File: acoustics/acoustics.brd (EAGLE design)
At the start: 160 x 100 mm, 172 parts, among them X1 22-23-2021, X2 22-23-2021, X3 22-23-2021

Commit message: Combining AGND and GND into one
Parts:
- removed C1, C10, C11, C12, C13, C14, C2, C3, C4, C47, C5, C6, C7, C9: 1uf, rcl:C0805K
- removed C48, C8: 10uf, rcl:C0805K
- removed C74, C76: 0.1uf, rcl:C0805K
- removed C75, C77: 47uf, rcl:C0805K
- removed R1, R2: 60.4k, rcl:M0805
- removed R3, R4: 10K, rcl:M0805
- removed R67, R68: 121k, resistor:R0603
- removed R71, R72: 47m, resistor:R0603
- added H2ADC_C9, H3ADC_C9: 0.1uf, rcl:C0603
- added H2RF_C1, H3RF_C1: 10uf, rcl:C0603
- added H2RF_C4, H2_C1, H2_C11, H2_C2, H2_C25, H2_C27, H2_C6, H3RF_C4, H3_ADC_C5, H3_C1, H3_C11, H3_C2, H3_C25, H3_C27: 1uf, rcl:C0603
- added H2RF_C6, H3RF_C6: 47uf, rcl:C0603
- added H2RF_R3, H3RF_R3: 121k, resistor:R0603
- added H2RF_RO, H3RF_RO: 47m, resistor:R0603
- added H2_R7, H3_R7: 60.4k, rcl:R0603
- added H2_R8, H3_R8: 10K, rcl:R0603
- moved U$10 292.7 mm to (71.6, 54.0)
- moved U$11 285.8 mm to (71.6, 30.6)
- moved H3CON 136.8 mm to (86.5, 41.1), turned to 270 degrees
- moved H2CON 133.1 mm to (86.5, 64.5), turned to 270 degrees
- moved ADC_H1 127.2 mm to (74.6, 92.6)
- moved ADC_H2 119.1 mm to (74.8, 65.4)
- moved ADC_H3 118.8 mm to (74.8, 42.1)
- moved U$2 35.2 mm to (-70.6, 47.6)
- moved H4_IN 29.9 mm to (39.5, 11.6), turned to 180 degrees
- moved H4_OUT 22.4 mm to (86.5, 18.3)
- moved H4PA_C_IN 22.2 mm to (38.3, 17.1), turned to 90 degrees
- moved ADC_H4 21.1 mm to (74.8, 19.1)
- moved H4DA_R_ON1 21.1 mm to (54.8, 20.6)
- moved H4DA_R_OP1 21.1 mm to (54.8, 18.7)
- moved H4RF_C_4 21.1 mm to (73.8, 6.03)
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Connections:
- new net N$37: ADC_H3.9, H3ADC_C9.2, H3RF_C6.2, U$11.5, U$11.6
- new net N$6: ADC_H1.9, C25.2, C73.2, U$1.5, U$1.6
- net +3V3: now also H2RF_C1.2, H2_C27.1, H2_C6.2, H3RF_C1.2, H3_ADC_C5.1, H3_C27.1; no longer C10.1, C11.2, C12.1, C13.1, C48.2, C8.2
- net AGND: no longer ADC_H1.10, ADC_H1.31, ADC_H1.5, ADC_H2.10, ADC_H2.31, ADC_H2.5, ADC_H3.10, ADC_H3.31, ADC_H3.5, ADC_H4.10, ADC_H4.31, ADC_H4.5, C1.1, C10.2, C11.1, C2.1, C22.1, C23.1, C24.2, C25.1, C26.2, C29.1, C3.1, C30.1, C31.1, C39.1, C4.2, C41.2, C47.1, C48.1, C54.1, C55.2, C6.1, C7.1, C74.1, C76.1, C8.1, C9.2, H4ADC_C.2, H4DA_R_IN1.1, H4RF_C_4.1, H4RF_C_IN.1, H4RF_C_O2.1, H4RF_R_0.1, H4RF_R_3.1, H4_C1.1, H4_C11.2, H4_C2.1, H4_DIFAMP.6, H4_IN.1, H4_PREAMP.2, H4_R6.2, H4_R7.2, H4_REFGEN.7, H4_REFGEN.8, HFPA_C.1, HFPA_C_INP.2, HFPA_R.2, R1.2, R15.1, R2.2, R24.2, R29.1, R3.2, R36.2, R4.2, R41.1, R65.1, R66.1, R67.1, R68.1, R7.2, R71.1, R72.1, R8.2, U$1.7, U$1.8, U$10.7, U$10.8, U$11.7, U$11.8, U$2.6, U$3.6, U$4.2, U$5.6, U$6.2, U$7.2, X1.1, X2.1, X3.1
- net GND: now also ADC_H1.10, ADC_H1.31, ADC_H1.5, ADC_H2.10, ADC_H2.12, ADC_H2.13, ADC_H2.14, ADC_H2.15, ADC_H2.16, ADC_H2.18, ADC_H2.21, ADC_H2.31, ADC_H2.5, ADC_H3.10, ADC_H3.12, ADC_H3.13, ADC_H3.14, ADC_H3.15, ADC_H3.16, ADC_H3.18, ADC_H3.21, ADC_H3.31, ADC_H3.5, ADC_H4.10, ADC_H4.31, ADC_H4.5, C22.1, C23.1, C24.2, C25.1, C26.2, C29.1, C30.1, C31.1, C39.1, C41.2, C54.1, C55.2, H2ADC_C9.1, H2RF_C1.1, H2RF_C4.1, H2RF_R3.1, H2RF_RO.1, H2_C1.1, H2_C11.2, H2_C2.1, H2_C25.1, H2_C27.2, H2_C6.1, H2_R7.2, H2_R8.2, H3ADC_C9.1, H3RF_C1.1, H3RF_C4.1, H3RF_R3.1, H3RF_RO.1, H3_ADC_C5.2, H3_C1.1, H3_C11.2, H3_C2.1, H3_C25.1, H3_C27.2, H3_R7.2, H3_R8.2, H4ADC_C.2, H4DA_R_IN1.1, H4RF_C_4.1, H4RF_C_IN.1, H4RF_C_O2.1, H4RF_R_0.1, H4RF_R_3.1, H4_C1.1, H4_C11.2, H4_C2.1, H4_DIFAMP.6, H4_IN.1, H4_PREAMP.2, H4_R6.2, H4_R7.2, H4_REFGEN.7, H4_REFGEN.8, HFPA_C.1, HFPA_C_INP.2, HFPA_R.2, R15.1, R24.2, R29.1, R36.2, R41.1, R65.1, R66.1, R7.2, R8.2, U$1.7, U$1.8, U$10.7, U$10.8, U$11.7, U$11.8, U$2.6, U$3.6, U$4.2, U$5.6, U$6.2, U$7.2, X1.1, X2.1, X3.1; no longer ADC_H4.24, C12.2, C13.2, C14.1, C5.1
- net N$1: now also H2_C1.2; no longer C2.2
- net N$12: now also H3_C1.2; no longer C7.2
- net N$13: now also H2_C25.2; no longer C5.2
- net N$18: now also H3_R7.1; no longer R2.1
- net N$21: now also H3_C11.1; no longer C9.1
- net N$22: now also H2_R8.1; no longer R3.1
- net N$23: now also H3_R8.1; no longer R4.1
- net N$3: now also H2_C2.2; no longer C1.2
- net N$30: now also H3_C25.2; no longer C14.2
- net N$4: now also H2_R7.1; no longer R1.1
- net N$42: now also H2RF_C4.2; no longer C3.2
- net N$43: now also H2RF_R3.2; no longer R67.2
- net N$47: now also H3RF_C4.2; no longer C47.2
- net N$79: now also H3RF_R3.2; no longer R68.2
- net N$8: now also H3_C2.2; no longer C6.2
- net N$86: now also H2RF_C6.1, H2RF_RO.2; no longer C75.1, R71.2
- net N$87: now also H3RF_C6.1, H3RF_RO.2; no longer C77.1, R72.2
- net N$9: now also H2_C11.1; no longer C4.1
- net POSITIVE_REF: now also H2ADC_C9.2, H2RF_C6.2; no longer ADC_H1.9, ADC_H3.9, C25.2, C73.2, C74.2, C75.2, C76.2, C77.2, U$1.5, U$1.6, U$11.5, U$11.6
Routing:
- net START: track 3.96 -> 85.5 mm, vias 1 -> 3
- net GND: track 12.7 -> 91.0 mm, vias 9 -> 74
- net SCLK: track 5.90 -> 79.9 mm, vias 1 -> 3
- net AGND: track 22.5 -> 0.00 mm, vias 21 -> 0
- net +3V3: track 15.0 -> 36.0 mm, vias 9 -> 21
- net DRDY_H3: track 0.00 -> 7.88 mm
- net DRDY_H2: track 0.00 -> 7.88 mm
- net DOUT_H2: track 0.00 -> 7.82 mm
- net DOUT_H3: track 0.00 -> 7.75 mm
- net N$54: track 10.0 -> 2.82 mm
- net N$37: track 0.00 -> 7.20 mm
- net POSITIVE_REF: track 0.00 -> 5.52 mm
- net N$71: track 8.57 -> 3.85 mm
- net DOUT_H4: track 10.1 -> 7.82 mm
- net DRDY_H4: track 9.97 -> 7.91 mm
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- removed copper zone on layer 2, net AGND
- removed copper zone on layer 2, net GND
- removed copper zone on layer 15, net N$37
- removed copper zone on layer 16, net N$41
- removed copper zone on layer 1, net N$88
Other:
- board size 160 x 100 mm -> 127 x 101.6 mm

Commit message: Initial placement of parts completed
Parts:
- removed C22, C23, C24, C26, C27, C28, C29: 1uf, rcl:C0805K
- removed C25: 0.1uf, rcl:C0805K
- removed C30: 10uf, rcl:C0805K
- removed C31, C39, C54: 100nF, resistor:C0603
- removed C32, C36, C44, C45, C58, C59: 270pF, resistor:C0603
- removed C33, C41, C55: 10mF, resistor:C0603
- removed C34, C42, C56: 1pF, resistor:C0603
- removed C35, C43, C57: 5nF, resistor:C0603
- removed C37, C46, C60: 1nF, resistor:C0603
- removed C38, C53, C61: 470 pF, resistor:C0603
- removed C40, C62, C71: 22nF, resistor:C0603
- removed C73: 47uf, rcl:C0805K
- removed R10, R16, R27, R30, R39, R42: 330, resistor:R0603
- removed R11, R12, R24, R25, R36, R37: 100k, resistor:R0603
- removed R13, R26, R38: 10k, resistor:R0603
- removed R14, R28, R40: 1.2K, resistor:R0603
- removed R15, R21, R22, R29, R33, R34, R41, R45, R46: 1.2k, resistor:R0603
- removed R17, R19, R31, R32, R43, R44: 5, resistor:R0603
- removed R18, R20, R47, R48, R61, R62: 10, resistor:R0603
- removed R23, R35, R9: 1 M, resistor:R0603
- removed R65: 121k, resistor:R0603
- removed R66: 47m, resistor:R0603
- removed R7: 60.4k, rcl:M0805
- removed R8: 10K, rcl:M0805
- removed U$2, U$3, U$5: THS4551, THS4551:VSSOP-8
- removed U$4, U$6, U$7: TLV6741, lio:SC70-5
- removed X1, X2, X3: 22-23-2021, con-molex:22-23-2021
- added H1ADC_C1, H1ADC_C11, H1ADC_C2, H1ADC_C25, H1ADC_C27, H1ADC_C6, H1RF_C4: 1uf, rcl:C0603
- added H1ADC_C9: 0.1uf, rcl:C0603
- added H1ADC_R7: 60.4k, rcl:R0603
- added H1ADC_R8: 10K, rcl:R0603
- added H1DA, H2DA, H3DA: THS4551, THS4551:VSSOP-8
- added H1DA_CO, H2DA_CO, H3DA_CO: 22nF, resistor:C0603
- added H1DA_C_I1, H2DA_C_I1, H3DA_C_I1: 470 pF, resistor:C0603
- added H1DA_C_I2, H2DA_C_I2, H3DA_C_I2: 1nF, resistor:C0603
- added H1DA_C_OFN, H1DA_C_OFP, H2DA_C_OFN, H2DA_C_OFP, H3DA_C_OFN, H3DA_C_OFP: 270pF, resistor:C0603
- added H1DA_R_IN1, H1DA_R_OFN, H1DA_R_OFP, H2DA_R_IN1, H2DA_R_OFN, H2DA_R_OFP, H3DA_R_IN1, H3DA_R_OFN, H3DA_R_OFP: 1.2k, resistor:R0603
- added H1DA_R_IN2, H1DA_R_IP2, H2DA_R_IN2, H2DA_R_IP2, H3DA_R_IN2, H3DA_R_IP2: 330, resistor:R0603
- added H1DA_R_IP1, H2DA_R_IP1, H3DA_R_IP1: 1.2K, resistor:R0603
- added H1DA_R_ON1, H1DA_R_OP1, H2DA_R_ON1, H2DA_R_OP1, H3DA_R_ON1, H3DA_R_OP1: 5, resistor:R0603
- added H1DA_R_ON2, H1DA_R_OP2, H2DA_R_ON2, H2DA_R_OP2, H3DA_R_ON2, H3DA_R__OP2: 10, resistor:R0603
- added H1PA, H2PA, H3PA: TLV6741, lio:SC70-5
- added H1PA_C, H2PA_C, H3PA_C: 100nF, resistor:C0603
- added H1PA_C_FB, H2PA_C_FB, H3PA_C_FB: 1pF, resistor:C0603
- added H1PA_C_IN, H2PA_C_IN, H3PA_C_IN: 5nF, resistor:C0603
- added H1PA_C_INP, H2PA_C_INP, H3PA_C_INP: 10mF, resistor:C0603
- added H1PA_R, H1PA_R2, H2PA_R, H2PA_R2, H3PA_R, H3PA_R2: 100k, resistor:R0603
- added H1PA_R_FB, H2PA_R_FB, H3PA_R_FB: 1 M, resistor:R0603
- added H1PA_R_IN, H2PA_R_IN, H3PA_R_IN: 10k, resistor:R0603
- added H1RF_C1: 10uf, rcl:C0603
- added H1RF_C6: 47uf, rcl:C0603
- added H1RF_R3: 121k, resistor:R0603
- added H1RF_RO: 47m, resistor:R0603
- added H1_IN, H2_IN, H3_IN: 22-23-2021, con-molex:22-23-2021
- moved H1CON 137.7 mm to (90.3, 88.3), turned to 270 degrees
- moved U$1 105.6 mm to (71.6, 77.6)
- moved H2CON 4.30 mm to (90.8, 64.8)
- moved ADC_H1 3.50 mm to (74.8, 89.1)
- moved H3CON 2.09 mm to (88.6, 41.4)
- moved H4_OUT 1.75 mm to (88.3, 18.3)
- moved H2_C2 0.32 mm to (67.8, 68.1)
- moved H2ADC_C9 0.32 mm to (71.4, 59.5)
- moved H2RF_C1 0.32 mm to (68.4, 52.1)
- moved H2RF_C4 0.32 mm to (74.0, 52.9)
- moved H2RF_C6 0.32 mm to (71.4, 58.1)
- moved H2RF_R3 0.32 mm to (71.0, 50.2)
- moved H2RF_RO 0.32 mm to (68.7, 57.3)
- moved H2_C11 0.32 mm to (73.8, 59.1)
- moved H2_R7 0.32 mm to (67.9, 64.1)
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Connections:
- removed net AGND: C33.2, R11.2
- new net CLK: ADC_H1.24, ADC_H2.24, ADC_H3.24, ADC_H4.24
- net +3V3: now also H1ADC_C27.1, H1ADC_C6.1, H1DA.3, H1PA.5, H1PA_C.2, H1PA_R2.2, H1RF_C1.2, H2DA.3, H2PA.5, H2PA_C.2, H2PA_R2.2, H3DA.3, H3PA.5, H3PA_C.2, H3PA_R2.2; no longer C24.1, C27.1, C30.2, C31.2, C39.2, C54.2, R12.2, R25.2, R37.2, U$2.3, U$3.3, U$4.5, U$5.3, U$6.5, U$7.5
- net ACD2_IN+: now also H2DA_CO.2, H2DA_R_OP2.2; no longer C62.2, R48.2
- net ACD3_IN+: now also H3DA_CO.2, H3DA_R__OP2.2; no longer C71.2, R62.2
- net ADC1_IN+: now also H1DA_CO.2, H1DA_R_OP2.2; no longer C40.2, R20.2
- net ADC1_IN-: now also H1DA_CO.1, H1DA_R_ON2.2; no longer C40.1, R18.2
- net ADC2_IN-: now also H2DA_CO.1, H2DA_R_ON2.2; no longer C62.1, R47.2
- net ADC3_IN-: now also H3DA_CO.1, H3DA_R_ON2.2; no longer C71.1, R61.2
- net GND: now also ADC_H1.12, ADC_H1.13, ADC_H1.14, ADC_H1.15, ADC_H1.16, ADC_H1.18, ADC_H1.21, H1ADC_C1.1, H1ADC_C11.2, H1ADC_C2.1, H1ADC_C25.1, H1ADC_C27.2, H1ADC_C6.2, H1ADC_C9.1, H1ADC_R7.2, H1ADC_R8.2, H1DA.6, H1DA_R_IN1.1, H1PA.2, H1PA_C.1, H1PA_C_INP.2, H1PA_R.2, H1RF_C1.1, H1RF_C4.1, H1RF_R3.1, H1RF_RO.1, H1_IN.1, H2DA.6, H2DA_R_IN1.1, H2PA.2, H2PA_C.1, H2PA_C_INP.2, H2PA_R.2, H2_IN.1, H3DA.6, H3DA_R_IN1.1, H3PA.2, H3PA_C.1, H3PA_C_INP.2, H3PA_R.2, H3_IN.1; no longer C22.1, C23.1, C24.2, C25.1, C26.2, C27.2, C28.1, C29.1, C30.1, C31.1, C39.1, C41.2, C54.1, C55.2, R15.1, R24.2, R29.1, R36.2, R41.1, R65.1, R66.1, R7.2, R8.2, U$2.6, U$3.6, U$4.2, U$5.6, U$6.2, U$7.2, X1.1, X2.1, X3.1
- net N$10: now also H1DA.5, H1DA_C_OFN.2, H1DA_R_ON1.1; no longer C32.2, R17.1, U$2.5
- net N$14: now also H2PA_C_IN.1, H2_IN.2; no longer C43.1, X2.2
- net N$15: now also H1PA.3, H1PA_C_FB.1, H1PA_R_FB.1, H1PA_R_IN.2; no longer C34.1, R13.2, R9.1, U$6.3
- net N$16: now also H1DA.8, H1DA_C_I2.1, H1DA_C_OFN.1, H1DA_R_IP2.2; no longer C32.1, C37.1, R10.2, U$2.8
- net N$17: now also H1DA.1, H1DA_C_I2.2, H1DA_C_OFP.1, H1DA_R_IN2.2; no longer C36.1, R16.2, U$2.1
- net N$19: now also H1DA_R_OFN.2, H1DA_R_ON1.2, H1DA_R_ON2.1; no longer R17.2, R18.1, R21.2
- net N$2: now also H1RF_C4.2; no longer C29.2
- net N$20: now also H1DA_C_I1.1, H1DA_R_IP1.2, H1DA_R_IP2.1, H1DA_R_OFN.1; no longer C38.1, R10.1, R14.2, R21.1
- net N$25: now also H1DA_C_I1.2, H1DA_R_IN1.2, H1DA_R_IN2.1, H1DA_R_OFP.1; no longer C38.2, R15.2, R16.1, R22.1
- net N$26: now also H1DA.4, H1DA_C_OFP.2, H1DA_R_OP1.1; no longer C36.2, R19.1, U$2.4
- net N$27: now also H1DA_R_OFP.2, H1DA_R_OP1.2, H1DA_R_OP2.1; no longer R19.2, R20.1, R22.2
- net N$28: now also H2PA_C_IN.2, H2PA_R_IN.1; no longer C43.2, R26.1
- net N$29: now also H2PA.3, H2PA_C_FB.1, H2PA_R_FB.1, H2PA_R_IN.2; no longer C42.1, R23.1, R26.2, U$4.3
- net N$33: now also H2DA.5, H2DA_C_OFN.2, H2DA_R_ON1.1; no longer C44.2, R31.1, U$3.5
- net N$36: now also H2DA.8, H2DA_C_I2.1, H2DA_C_OFN.1, H2DA_R_IP2.2; no longer C44.1, C46.1, R27.2, U$3.8
- net N$39: now also H1ADC_C1.2; no longer C23.2
- net N$40: now also H1ADC_C2.2; no longer C22.2
- net N$44: now also H1ADC_R7.1; no longer R7.1
- net N$45: now also H1ADC_R8.1; no longer R8.1
- net N$46: now also H1RF_C6.1, H1RF_RO.2; no longer C73.1, R66.2
- net N$48: now also H1ADC_C11.1; no longer C26.1
- net N$49: now also H1PA.1, H1PA_C_INP.1, H1PA_R.1, H1PA_R2.1; no longer C33.1, R11.1, R12.1, U$6.1
- net N$5: now also H1PA_C_IN.1, H1_IN.2; no longer C35.1, X1.2
- net N$50: now also H2DA.1, H2DA_C_I2.2, H2DA_C_OFP.1, H2DA_R_IN2.2; no longer C45.1, R30.2, U$3.1
- net N$51: now also H2DA_C_I1.1, H2DA_R_IP1.2, H2DA_R_IP2.1, H2DA_R_OFN.1; no longer C53.1, R27.1, R28.2, R33.1
- net N$52: now also H2DA_C_I1.2, H2DA_R_IN1.2, H2DA_R_IN2.1, H2DA_R_OFP.1; no longer C53.2, R29.2, R30.1, R34.1
- net N$53: now also H2DA.4, H2DA_C_OFP.2, H2DA_R_OP1.1; no longer C45.2, R32.1, U$3.4
- net N$55: now also H2PA.1, H2PA_C_INP.1, H2PA_R.1, H2PA_R2.1; no longer C41.1, R24.1, R25.1, U$4.1
- net N$56: now also H1ADC_C25.2; no longer C28.2
- net N$57: now also H3PA_C_IN.1, H3_IN.2; no longer C57.1, X3.2
- net N$58: now also H3PA_C_IN.2, H3PA_R_IN.1; no longer C57.2, R38.1
- net N$59: now also H3PA.3, H3PA_C_FB.1, H3PA_R_FB.1, H3PA_R_IN.2; no longer C56.1, R35.1, R38.2, U$7.3
- net N$6: now also H1ADC_C9.2, H1RF_C6.2; no longer C25.2, C73.2
- net N$60: now also H3DA.5, H3DA_C_OFN.2, H3DA_R_ON1.1; no longer C58.2, R43.1, U$5.5
- net N$61: now also H1RF_R3.2; no longer R65.2
- net N$62: now also H3DA.8, H3DA_C_I2.1, H3DA_C_OFN.1, H3DA_R_IP2.2; no longer C58.1, C60.1, R39.2, U$5.8
- net N$63: now also H3DA.1, H3DA_C_I2.2, H3DA_C_OFP.1, H3DA_R_IN2.2; no longer C59.1, R42.2, U$5.1
- net N$64: now also H3DA_C_I1.1, H3DA_R_IP1.2, H3DA_R_IP2.1, H3DA_R_OFN.1; no longer C61.1, R39.1, R40.2, R45.1
- net N$65: now also H3DA_C_I1.2, H3DA_R_IN1.2, H3DA_R_IN2.1, H3DA_R_OFP.1; no longer C61.2, R41.2, R42.1, R46.1
- net N$66: now also H3DA.4, H3DA_C_OFP.2, H3DA_R_OP1.1; no longer C59.2, R44.1, U$5.4
- net N$68: now also H3PA.1, H3PA_C_INP.1, H3PA_R.1, H3PA_R2.1; no longer C55.1, R36.1, R37.1, U$7.1
- net N$69: now also H2DA_R_OFN.2, H2DA_R_ON1.2, H2DA_R_ON2.1; no longer R31.2, R33.2, R47.1
- net N$7: now also H1PA_C_IN.2, H1PA_R_IN.1; no longer C35.2, R13.1
- net N$70: now also H2DA_R_OFP.2, H2DA_R_OP1.2, H2DA_R_OP2.1; no longer R32.2, R34.2, R48.1
- net N$81: now also H3DA_R_OFN.2, H3DA_R_ON1.2, H3DA_R_ON2.1; no longer R43.2, R45.2, R61.1
- net N$82: now also H3DA_R_OFP.2, H3DA_R_OP1.2, H3DA_R__OP2.1; no longer R44.2, R46.2, R62.1
- net PA-A1+: now also H1DA_R_IP1.1, H1PA.4, H1PA_C_FB.2, H1PA_R_FB.2; no longer C34.2, R14.1, R9.2, U$6.4
- net PA-A1+1: now also H2DA_R_IP1.1, H2PA.4, H2PA_C_FB.2, H2PA_R_FB.2; no longer C42.2, R23.2, R28.1, U$4.4
- net PA-A1+2: now also H3DA_R_IP1.1, H3PA.4, H3PA_C_FB.2, H3PA_R_FB.2; no longer C56.2, R35.2, R40.1, U$7.4
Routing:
- net CLK: track 0.00 -> 85.8 mm, vias 0 -> 4
- net GND: track 91.0 -> 137.1 mm, vias 74 -> 115
- net +3V3: track 36.0 -> 58.8 mm, vias 21 -> 36
- net N$81: track 0.00 -> 11.8 mm
- net N$69: track 0.00 -> 11.8 mm
- net N$27: track 0.00 -> 11.8 mm
- net N$82: track 0.00 -> 11.8 mm
- net N$70: track 0.00 -> 11.8 mm
- net N$19: track 0.00 -> 11.6 mm
- net DOUT_H1: track 0.00 -> 11.3 mm
- net DRDY_H1: track 0.00 -> 11.3 mm
- net ADC1_IN+: track 0.00 -> 8.42 mm
- net ADC3_IN-: track 0.00 -> 8.29 mm
- net ACD3_IN+: track 0.00 -> 8.27 mm
- net ACD2_IN+: track 0.00 -> 8.27 mm
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- added copper zone on layer 2, net GND
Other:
- board size 127 x 101.6 mm -> 76.2 x 101.6 mm

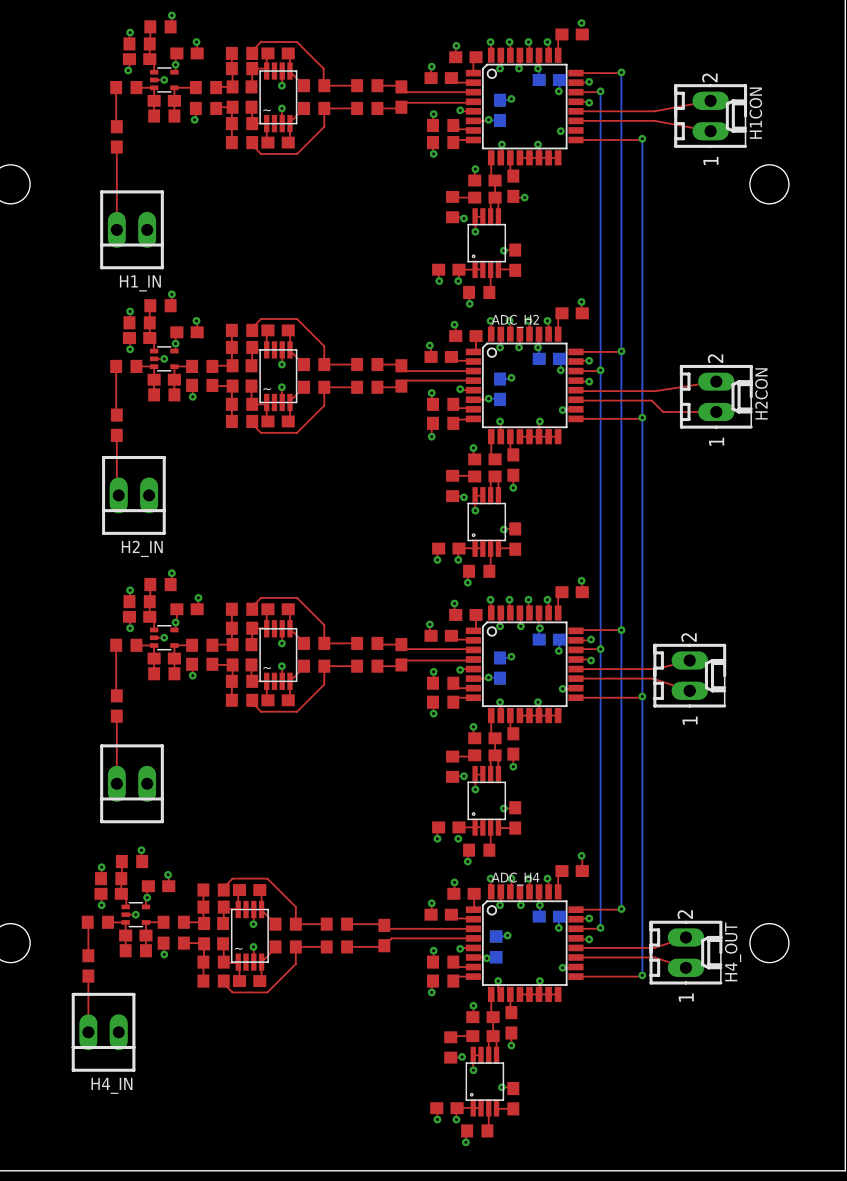
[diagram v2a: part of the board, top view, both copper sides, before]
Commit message: Fixing connector placement of signal connectors
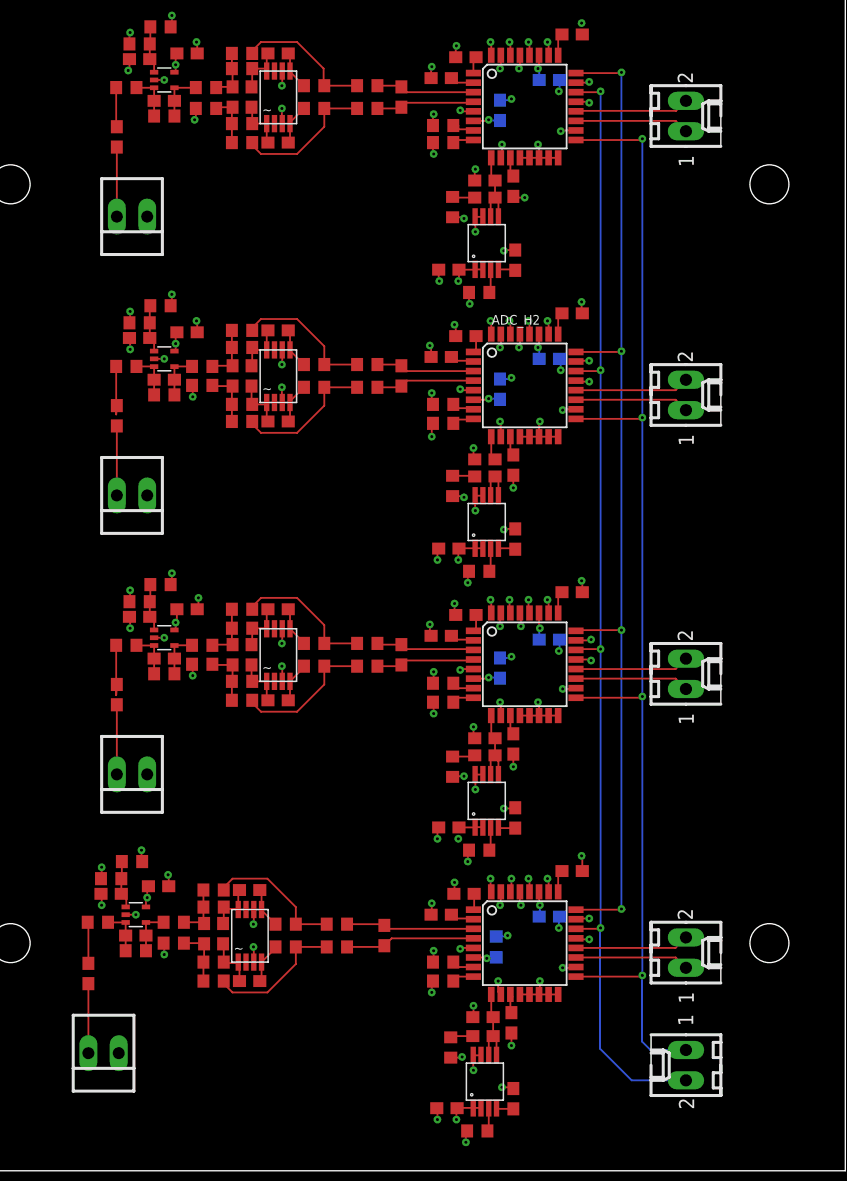
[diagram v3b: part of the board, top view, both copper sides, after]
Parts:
- added DCON: 22-27-2021-02, con-molex:6410-02
- moved H2CON 2.54 mm to (88.3, 64.9)
- moved H1CON 2.06 mm to (88.3, 88.3)
- moved H4_IN 1.75 mm to (39.5, 9.84)
- moved H1_IN 1.11 mm to (41.9, 79.9)
- moved H3PA_C_IN 0.95 mm to (40.6, 39.8)
- moved H2PA_C_IN 0.79 mm to (40.6, 63.2)
- moved H3_IN 0.79 mm to (41.9, 33.2)
- moved H4PA_C_IN 0.63 mm to (38.3, 16.5)
- moved H3CON 0.35 mm to (88.3, 41.6)
- moved H2_IN 0.16 mm to (41.9, 56.5)
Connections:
- net SCLK: now also DCON.2
- net START: now also DCON.1
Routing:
- net SCLK: track 78.5 -> 96.9 mm
- net START: track 92.4 -> 101.9 mm
- net DRDY_H2: track 12.2 -> 9.56 mm
- net DOUT_H2: track 11.8 -> 9.56 mm
- net DRDY_H1: track 11.3 -> 9.56 mm
- net DOUT_H1: track 11.3 -> 9.56 mm
- net GND: track 137.1 -> 138.4 mm, vias 115 -> 116
- net N$5: track 6.93 -> 5.82 mm
- net N$34: track 4.71 -> 5.82 mm
- net N$58: track 4.25 -> 5.07 mm
- net N$14: track 5.09 -> 5.82 mm
- net N$28: track 4.09 -> 4.75 mm
- net N$54: track 2.82 -> 3.46 mm

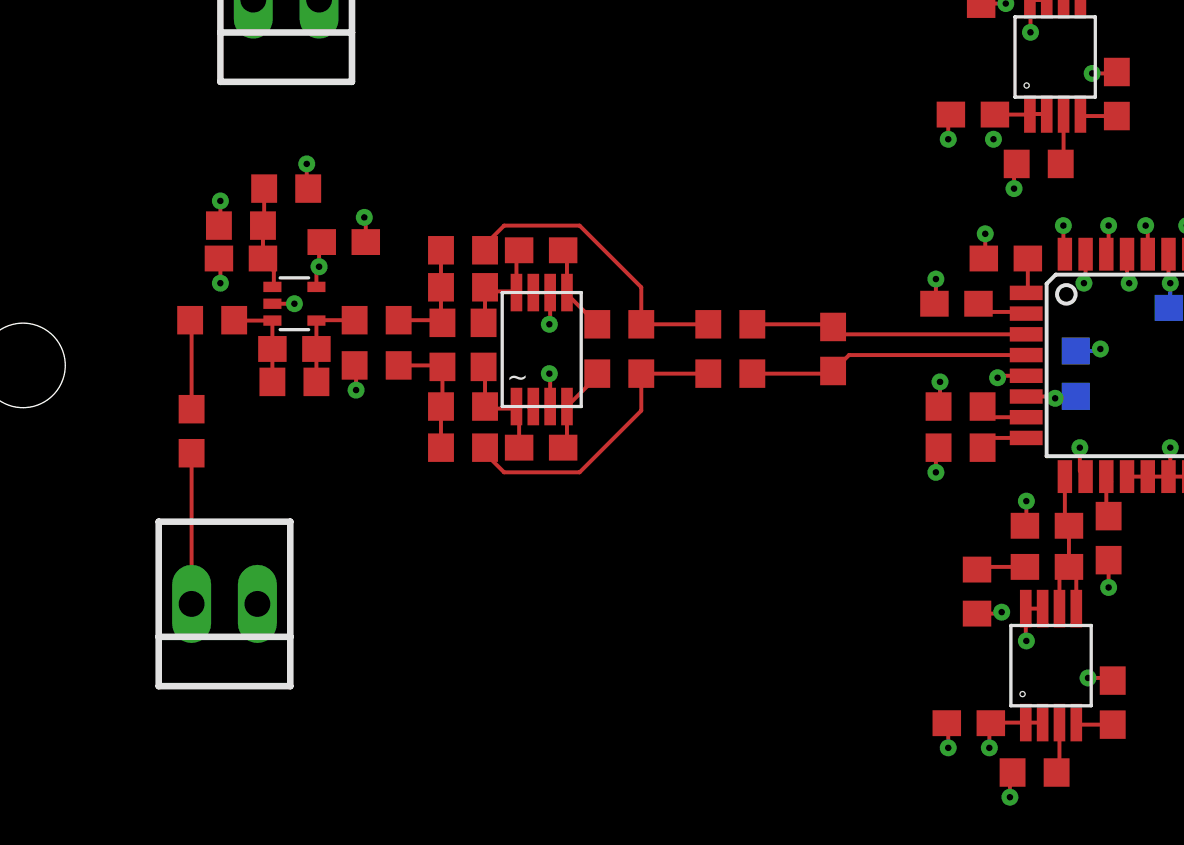
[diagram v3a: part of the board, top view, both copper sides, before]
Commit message: Fixing channel 4 to match the others
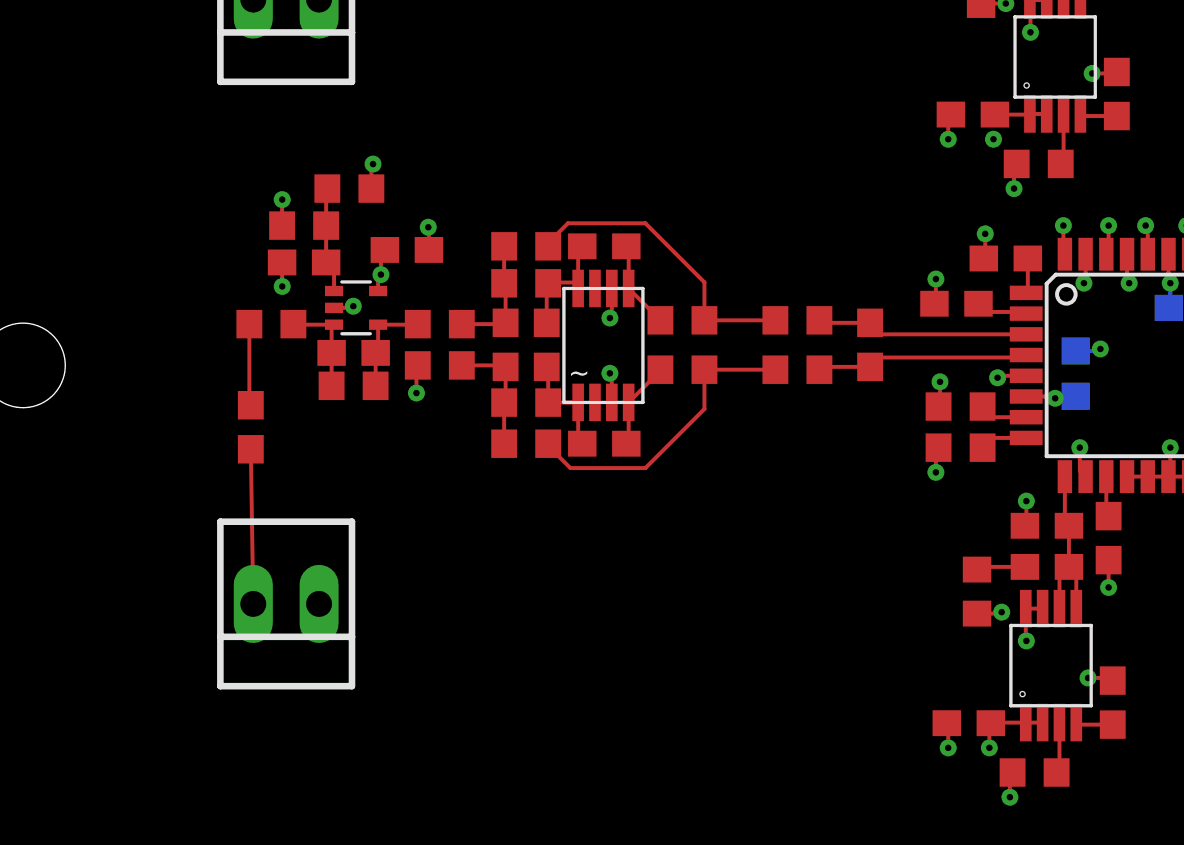
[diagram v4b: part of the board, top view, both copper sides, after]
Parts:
- moved H4DA_R_ON2 2.60 mm to (61.6, 20.8)
- moved H4DA_R_OP2 2.60 mm to (61.6, 18.9)
- moved HFPA_C 2.46 mm to (46.6, 23.5)
- moved H4DA_C_OFN 2.44 mm to (54.2, 23.6)
- moved H4DA_C_OFP 2.44 mm to (54.2, 16.0)
- moved H4DA_R_IN2 2.44 mm to (51.2, 17.6)
- moved H4DA_R_IP2 2.44 mm to (51.2, 22.2)
- moved H4DA_R_OFN 2.44 mm to (51.2, 23.6)
- moved H4DA_R_OFP 2.44 mm to (51.2, 16.0)
- moved H4DA_R_ON1 2.44 mm to (57.2, 20.8)
- moved HFPA_C_INP 2.44 mm to (42.6, 23.0)
- moved H4DA_R_OP1 2.44 mm to (57.2, 18.9)
- moved H4DA_R_IP1 2.44 mm to (47.8, 20.6)
- moved H4DA_CI2 2.44 mm to (52.0, 19.8)
- moved HFPA_R 2.44 mm to (42.6, 24.4)
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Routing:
- net ACD4_IN+: track 10.9 -> 8.24 mm
- net ADC4_IN-: track 10.7 -> 8.21 mm
- net +3V3: track 58.8 -> 58.3 mm
